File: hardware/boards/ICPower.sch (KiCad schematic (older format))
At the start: 47 parts, among them U1 ECP5UM5G-381caBGA, U3 CYUSB3014, U4 IS43TR16256B-125KBL, U5 128MiB, U6 128MiB, U7 SI5330B

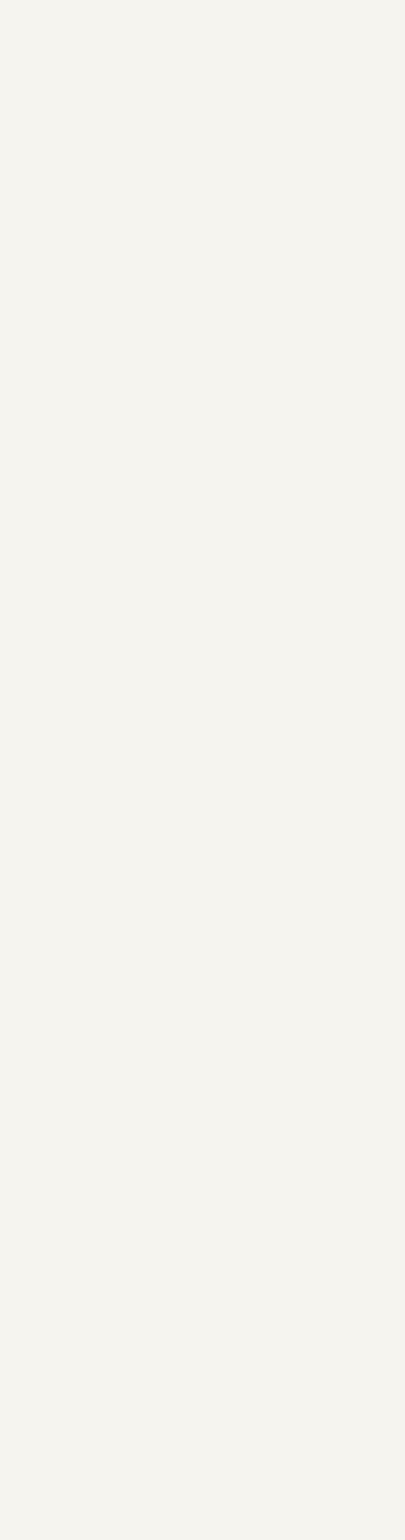
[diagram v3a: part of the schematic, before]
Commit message: Added the debug module connector (SODIMM 260), it's not hooked up to anything yet
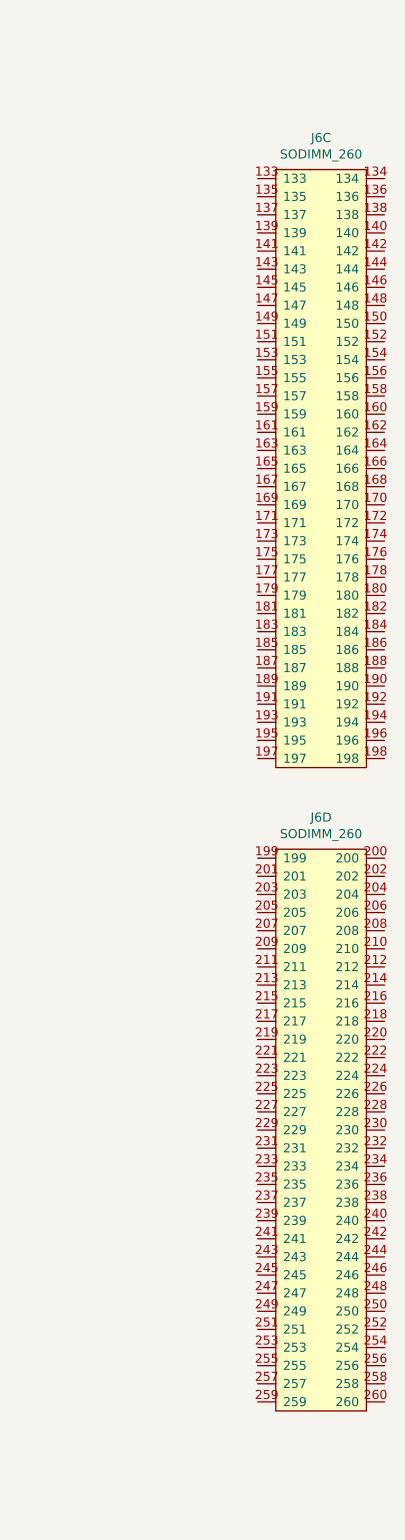
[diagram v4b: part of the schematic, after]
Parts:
- added J6: SODIMM_260, lethalbit-connectors:TE_SODIMM_260, symbol lethalbit:SODIMM_260
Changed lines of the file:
@@
 	9100 2750 9600 2750
 NoConn ~ 9100 2600
+$Comp
+L lethalbit:SODIMM_260 J6
+U 3 1 5F2B0555
+P 14400 2950
+F 0 "J6" H 14400 3525 50  0000 C CNN
+F 1 "SODIMM_260" H 14400 3434 50  0000 C CNN
+F 2 "lethalbit-connectors:TE_SODIMM_260" H 14400 3300 50  0001 C CNN
+F 3 "https://www.te.com/commerce/DocumentDelivery/DDEController?Action=srchrtrv&DocNm=2309413&DocType=Customer+Drawing&DocLang=English" H 14400 3300 50  0001 C CNN
+F 4 "TE Connectivity AMP Connectors" H 14400 2950 50  0001 C CNN "MFR"
+F 5 "2309413-1" H 14400 2950 50  0001 C CNN "MPN"
+	3    14400 2950
+	1    0    0    -1
+$EndComp
+$Comp
+L lethalbit:SODIMM_260 J6
+U 4 1 5F2B71A4
+P 14400 6700
+F 0 "J6" H 14400 7275 50  0000 C CNN
+F 1 "SODIMM_260" H 14400 7184 50  0000 C CNN
+F 2 "lethalbit-connectors:TE_SODIMM_260" H 14400 7050 50  0001 C CNN
+F 3 "https://www.te.com/commerce/DocumentDelivery/DDEController?Action=srchrtrv&DocNm=2309413&DocType=Customer+Drawing&DocLang=English" H 14400 7050 50  0001 C CNN
+F 4 "TE Connectivity AMP Connectors" H 14400 6700 50  0001 C CNN "MFR"
+F 5 "2309413-1" H 14400 6700 50  0001 C CNN "MPN"
+	4    14400 6700
+	1    0    0    -1
+$EndComp
 $EndSCHEMATC
